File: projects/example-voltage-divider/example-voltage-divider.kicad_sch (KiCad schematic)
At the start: 2 parts

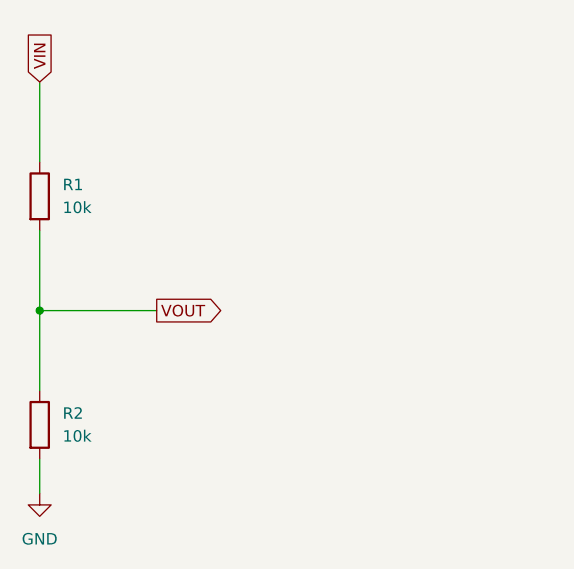
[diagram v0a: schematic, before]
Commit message: Pin toolchain to stable KiCad 9.0.x and make reference project ERC-clean
- setup.sh: install KiCad 9.0.x from official PPA (was Ubuntu's 7.0.11),
  configurable via KICAD_PPA; seed global sym/fp lib tables for headless ERC
- export.sh: add ERC report (kicad-cli sch erc, KiCad 8+) to the pipeline
- example-voltage-divider: add PWR_FLAG + 3-pin I/O connector (J1) and fix
  off-grid endpoint so the reference passes ERC with 0 errors
- README: document team-wide KiCad version pinning (stable, not nightly)
- gitignore KiCad editor lock files

Co-authored-by: IMasliukou <IMasliukou@users.noreply.github.com>
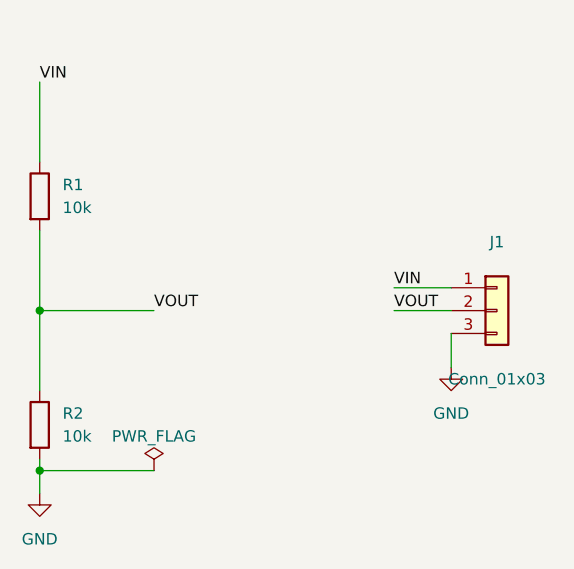
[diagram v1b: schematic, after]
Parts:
- added J1: Conn_01x03, symbol Connector_Generic:Conn_01x03
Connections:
- net GND: now also J1.3 (Pin_3)
- net VIN: now also J1.1 (Pin_1)
- net VOUT: now also J1.2 (Pin_2)
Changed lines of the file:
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@@
     (stroke (width 0) (type default))
   )
-  (wire (pts (xy 127 76.2) (xy 140 76.2))
+  (wire (pts (xy 127 76.2) (xy 139.7 76.2))
     (stroke (width 0) (type default))
   )
-  (wire (pts (xy 127 92.71) (xy 127 96.52))
+  (wire (pts (xy 127 92.71) (xy 127 93.98))
     (stroke (width 0) (type default))
   )
-  (global_label "VIN" (shape input) (at 127 50.8 90) (fields_autoplaced)
-    (effects (font (size 1.27 1.27)) (justify left))
-    (property "Intersheetrefs" "${INTERSHEET_REFS}" (at 0 0 0)
-      (effects (font (size 1.27 1.27)) hide)
-    )
+  (wire (pts (xy 127 93.98) (xy 127 96.52))
+    (stroke (width 0) (type default))
   )
-  (global_label "VOUT" (shape output) (at 140 76.2 0) (fields_autoplaced)
-    (effects (font (size 1.27 1.27)) (justify left))
-    (property "Intersheetrefs" "${INTERSHEET_REFS}" (at 0 0 0)
-      (effects (font (size 1.27 1.27)) hide)
-    )
+  (wire (pts (xy 127 93.98) (xy 139.7 93.98))
+    (stroke (width 0) (type default))
+  )
+  (junction (at 127 93.98) (diameter 0) (color 0 0 0 0)
+  )
+  (label "VIN" (at 127 50.8 0) (fields_autoplaced)
+    (effects (font (size 1.27 1.27)) (justify left bottom))
+  )
+  (label "VOUT" (at 139.7 76.2 0) (fields_autoplaced)
+    (effects (font (size 1.27 1.27)) (justify left bottom))
   )
   (symbol (lib_id "Device:R") (at 127 63.5 0) (unit 1)
@@
         )
       )
+    )
+  )
+  (symbol (lib_id "power:PWR_FLAG") (at 139.7 93.98 0) (unit 1)
+    (in_bom yes) (on_board yes) (dnp no) (fields_autoplaced)
+    (property "Reference" "#FLG01" (at 139.7 92.075 0)
+      (effects (font (size 1.27 1.27)) hide)
+    )
+    (property "Value" "PWR_FLAG" (at 139.7 90.17 0)
+      (effects (font (size 1.27 1.27)))
+    )
+    (property "Footprint" "" (at 139.7 93.98 0)
+      (effects (font (size 1.27 1.27)) hide)
+    )
+    (property "Datasheet" "~" (at 139.7 93.98 0)
+      (effects (font (size 1.27 1.27)) hide)
+    )
+    (pin "1")
+    (instances
+      (project "example-voltage-divider"
+        (path "/5c2019fb-09d8-4b44-86b6-3a790e21cb99"
+          (reference "#FLG01") (unit 1)
+        )
+      )
+    )
+  )
+  (wire (pts (xy 166.37 73.66) (xy 172.72 73.66))
+    (stroke (width 0) (type default))
+  )
+  (wire (pts (xy 166.37 76.2) (xy 172.72 76.2))
+    (stroke (width 0) (type default))
+  )
+  (wire (pts (xy 172.72 78.74) (xy 172.72 82.55))
+    (stroke (width 0) (type default))
+  )
+  (label "VIN" (at 166.37 73.66 0) (fields_autoplaced)
+    (effects (font (size 1.27 1.27)) (justify left bottom))
+  )
+  (label "VOUT" (at 166.37 76.2 0) (fields_autoplaced)
+    (effects (font (size 1.27 1.27)) (justify left bottom))
+  )
+  (symbol (lib_id "Connector_Generic:Conn_01x03") (at 177.8 76.2 0) (unit 1)
+    (in_bom yes) (on_board yes) (dnp no) (fields_autoplaced)
+    (property "Reference" "J1" (at 177.8 68.58 0)
+      (effects (font (size 1.27 1.27)))
+    )
+    (property "Value" "Conn_01x03" (at 177.8 83.82 0)
+      (effects (font (size 1.27 1.27)))
+    )
+    (property "Footprint" "" (at 177.8 76.2 0)
+      (effects (font (size 1.27 1.27)) hide)
+    )
+    (property "Datasheet" "~" (at 177.8 76.2 0)
+      (effects (font (size 1.27 1.27)) hide)
+    )
+    (pin "1")
+    (pin "2")
+    (pin "3")
+    (instances
+      (project "example-voltage-divider"
+        (path "/5c2019fb-09d8-4b44-86b6-3a790e21cb99"
+          (reference "J1") (unit 1)
+        )
+      )
+    )
+  )
+  (symbol (lib_id "power:GND") (at 172.72 82.55 0) (unit 1)
+    (in_bom yes) (on_board yes) (dnp no) (fields_autoplaced)
+    (property "Reference" "#PWR02" (at 172.72 88.9 0)
+      (effects (font (size 1.27 1.27)) hide)
+    )
+    (property "Value" "GND" (at 172.72 87.63 0)
+      (effects (font (size 1.27 1.27)))
+    )
+    (property "Footprint" "" (at 172.72 82.55 0)
+      (effects (font (size 1.27 1.27)) hide)
+    )
+    (property "Datasheet" "" (at 172.72 82.55 0)
+      (effects (font (size 1.27 1.27)) hide)
+    )
+    (pin "1")
+    (instances
+      (project "example-voltage-divider"
+        (path "/5c2019fb-09d8-4b44-86b6-3a790e21cb99"
+          (reference "#PWR02") (unit 1)
+        )
+      )
